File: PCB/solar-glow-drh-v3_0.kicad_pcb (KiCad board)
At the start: 2 copper layers, 50.8 x 88.9 mm, 67 parts, among them J1 UPDI hdr, Q1 BCP5316MTWG, SW2 LED master, U1 AVR64DD28 (VQFN28), U2 ALD910025SALI, U3 ADXL367, U4 TLV3011BIDBVR, U5 NT3H2211, U6 TPS22918

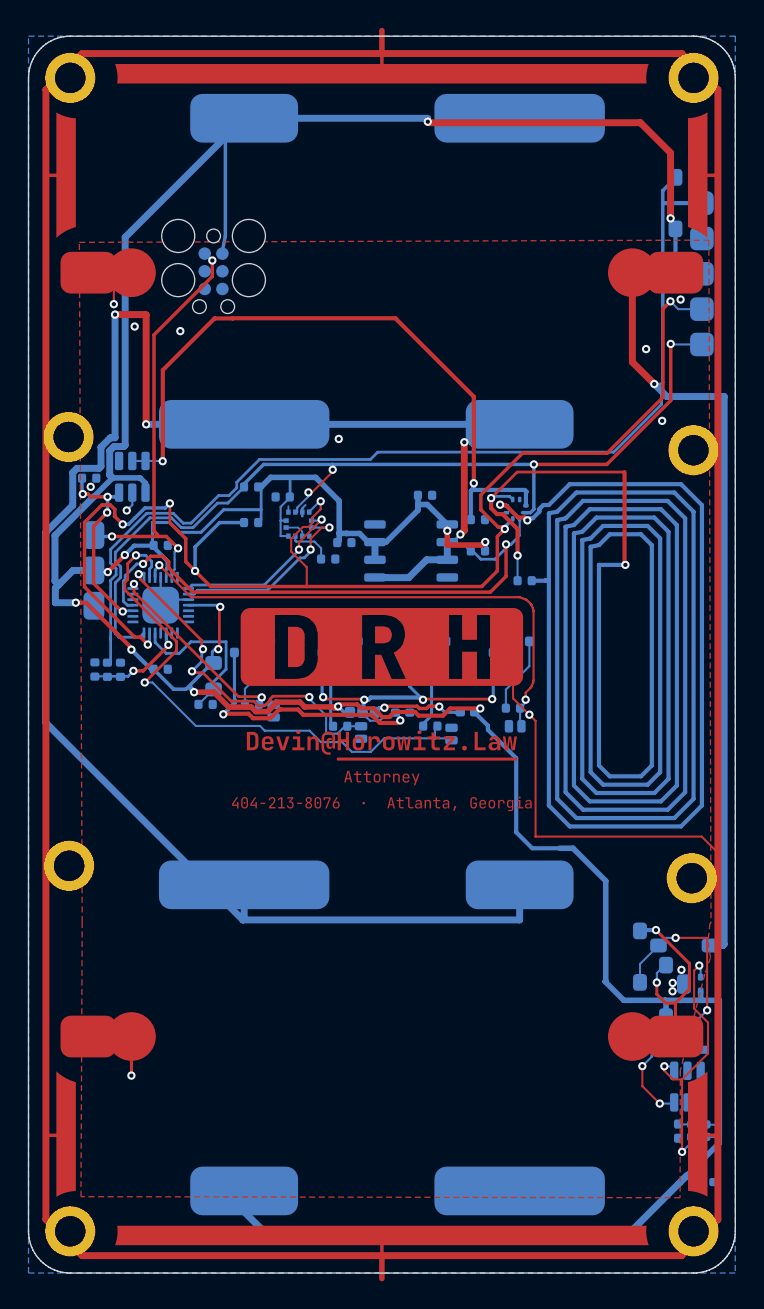
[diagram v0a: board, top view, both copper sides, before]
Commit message: PCB: nudge the 4 panel-corner mounting holes to a clean symmetric grid
The 4 GND mounting holes at the solar-panel inner corners were placed
roughly -- the two holes of each panel disagreed in y by ~0.9 mm. Snap
them to the corner-mount columns (x 3.0 / 47.8) at the panel inner edges
(y 28.5 / 60.4), giving a symmetric two-column, 8-hole pattern:

  W-PV1  (2.88, 28.81) -> (3.0, 28.5)
  E-PV1  (47.79, 29.76) -> (47.8, 28.5)
  W-PV2  (2.92, 59.63) -> (3.0, 60.4)
  E-PV2  (47.67, 60.52) -> (47.8, 60.4)

Holes are 3.6 mm copper / 2.2 mm drill, already on GND. At the new spots
the copper clears the board edge by 1.2 mm, the NFC coil keepout by
1.2-1.3 mm (the two east holes sit just N/S of it), and the nearest
non-GND pad (R14, D10) by >= 1.4 mm.

Follow-ups (not done here):
- Zones need a refill in KiCad (no kicad-cli in this env) so the GND pour
  reconnects to the moved pads; then re-run DRC.
- The enclosure backshell defines only 4 bosses; add these 4 (x,y) to its
  mounts list so bosses grow under them.

Co-Authored-By: Claude Opus 4.8 <noreply@anthropic.com>
Claude-Session: https://claude.ai/code/session_01PBK3zFENdvoGtn8yP7qPA8
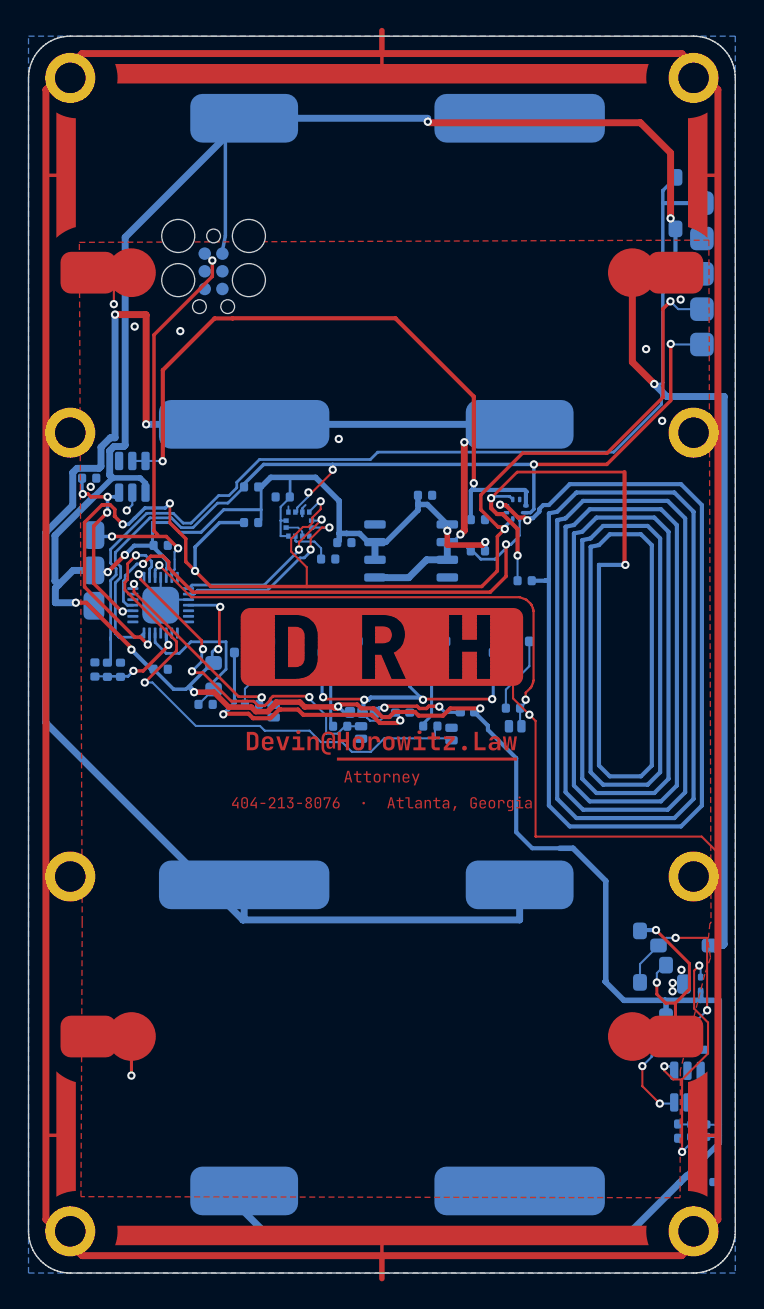
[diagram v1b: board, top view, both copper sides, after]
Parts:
- moved ? 1.26 mm to (47.8, 28.5)
- moved ? 0.77 mm to (3.00, 60.4)
- moved ? 0.33 mm to (3.00, 28.5)
- moved ? 0.18 mm to (47.8, 60.4)
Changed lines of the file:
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@@
 	(footprint ""
 		(layer "F.Cu")
-		(at 2.92 59.63)
+		(at 3 60.4)
 		(property "Reference" ""
 			(at 0 0 0)
@@
 	(footprint ""
 		(layer "F.Cu")
-		(at 47.67 60.52)
+		(at 47.8 60.4)
 		(property "Reference" ""
 			(at 0 0 0)
@@
 	(footprint ""
 		(layer "F.Cu")
-		(at 2.88 28.81)
+		(at 3 28.5)
 		(property "Reference" ""
 			(at 0 0 0)
@@
 	(footprint ""
 		(layer "F.Cu")
-		(at 47.79 29.76)
+		(at 47.8 28.5)
 		(property "Reference" ""
 			(at 0 0 0)
